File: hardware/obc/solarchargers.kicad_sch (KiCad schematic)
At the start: 35 parts, among them U105 LTC4121, U106 LTC4121

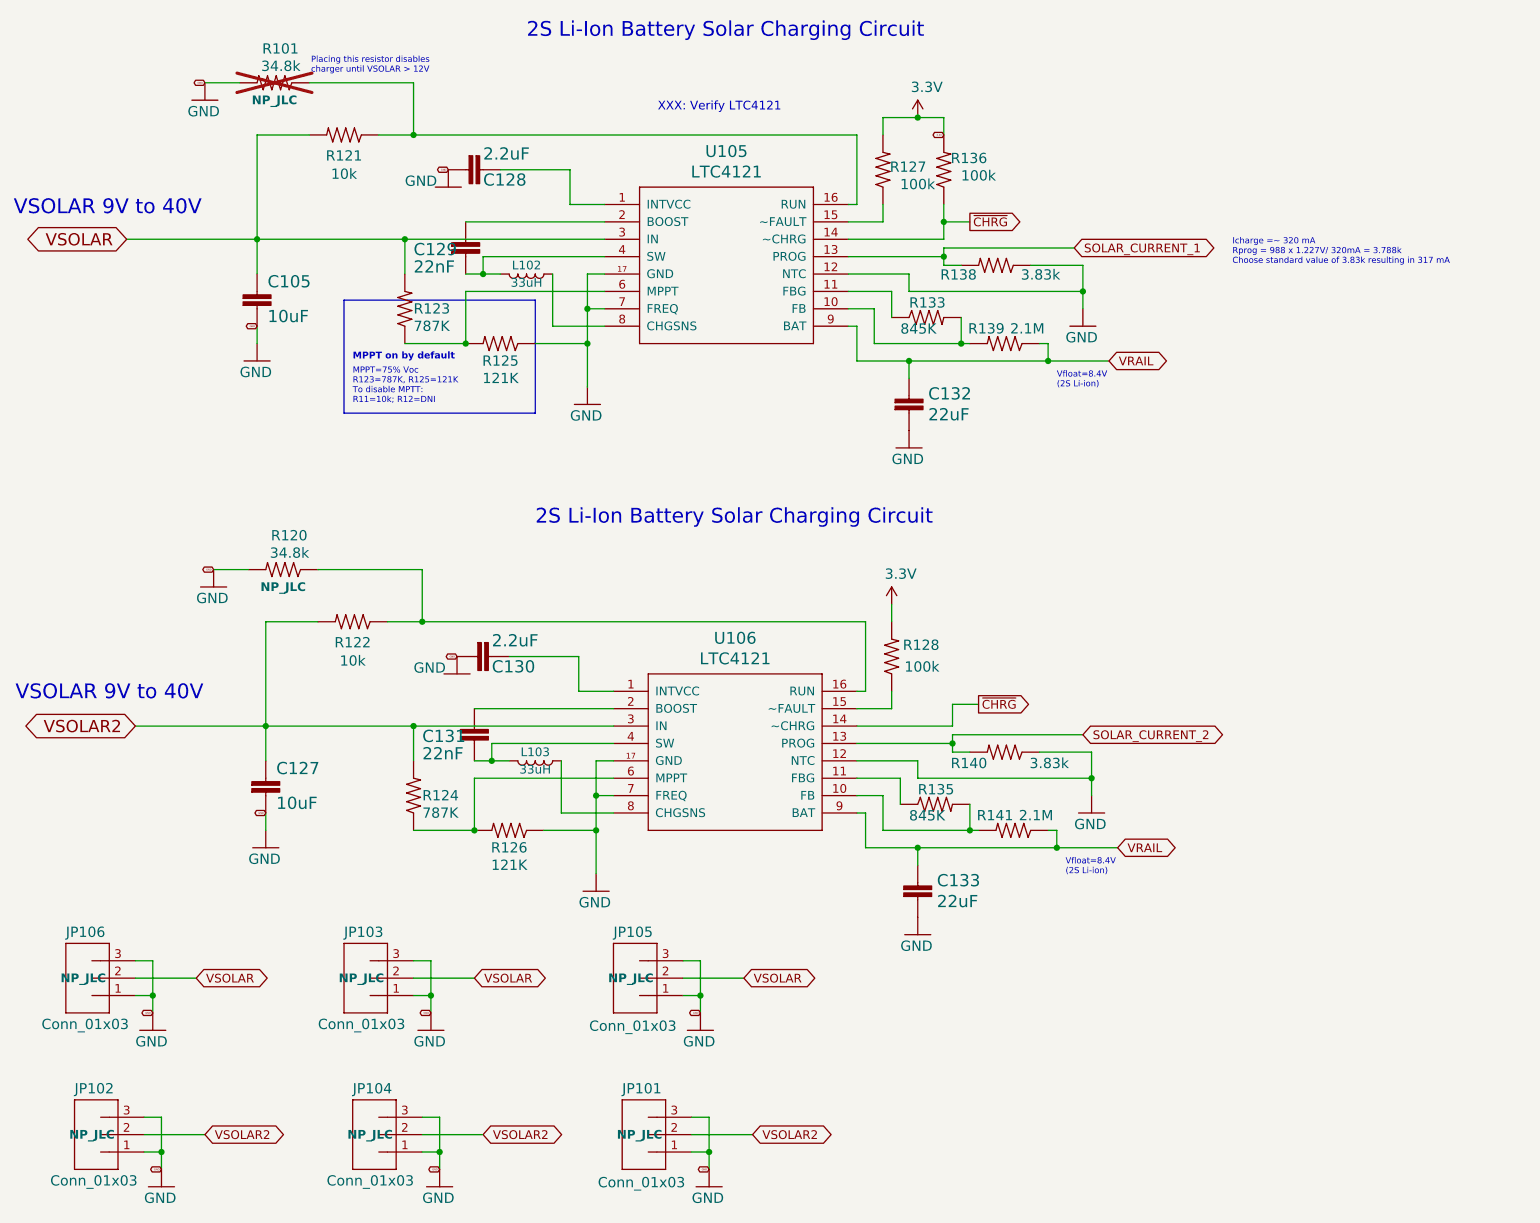
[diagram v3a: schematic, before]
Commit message: obc: design review and corrections
- text cleanup, put components on grid
- Re-route RF power network for radio to get thicker traces and lower
impedance.
- Route RF connections for GPS (controlled impedance)
- Lots of straightening and spreading traces and improving pours
(especially power paths).
- Swap pinning of RBF jumper to reduce the possible downsides of
any shorts or misconnections (don't put pack+ and pack- together on
the connector)
- geographical reannotate
- improve placement of a couple of bypass caps
- Adjust 10uF solar input capacitors to be 35V rated so as to not
limit input voltage.
- fix pinning of RF splitter
- add a couple of STEP models
- obc: add DQ1225 step model
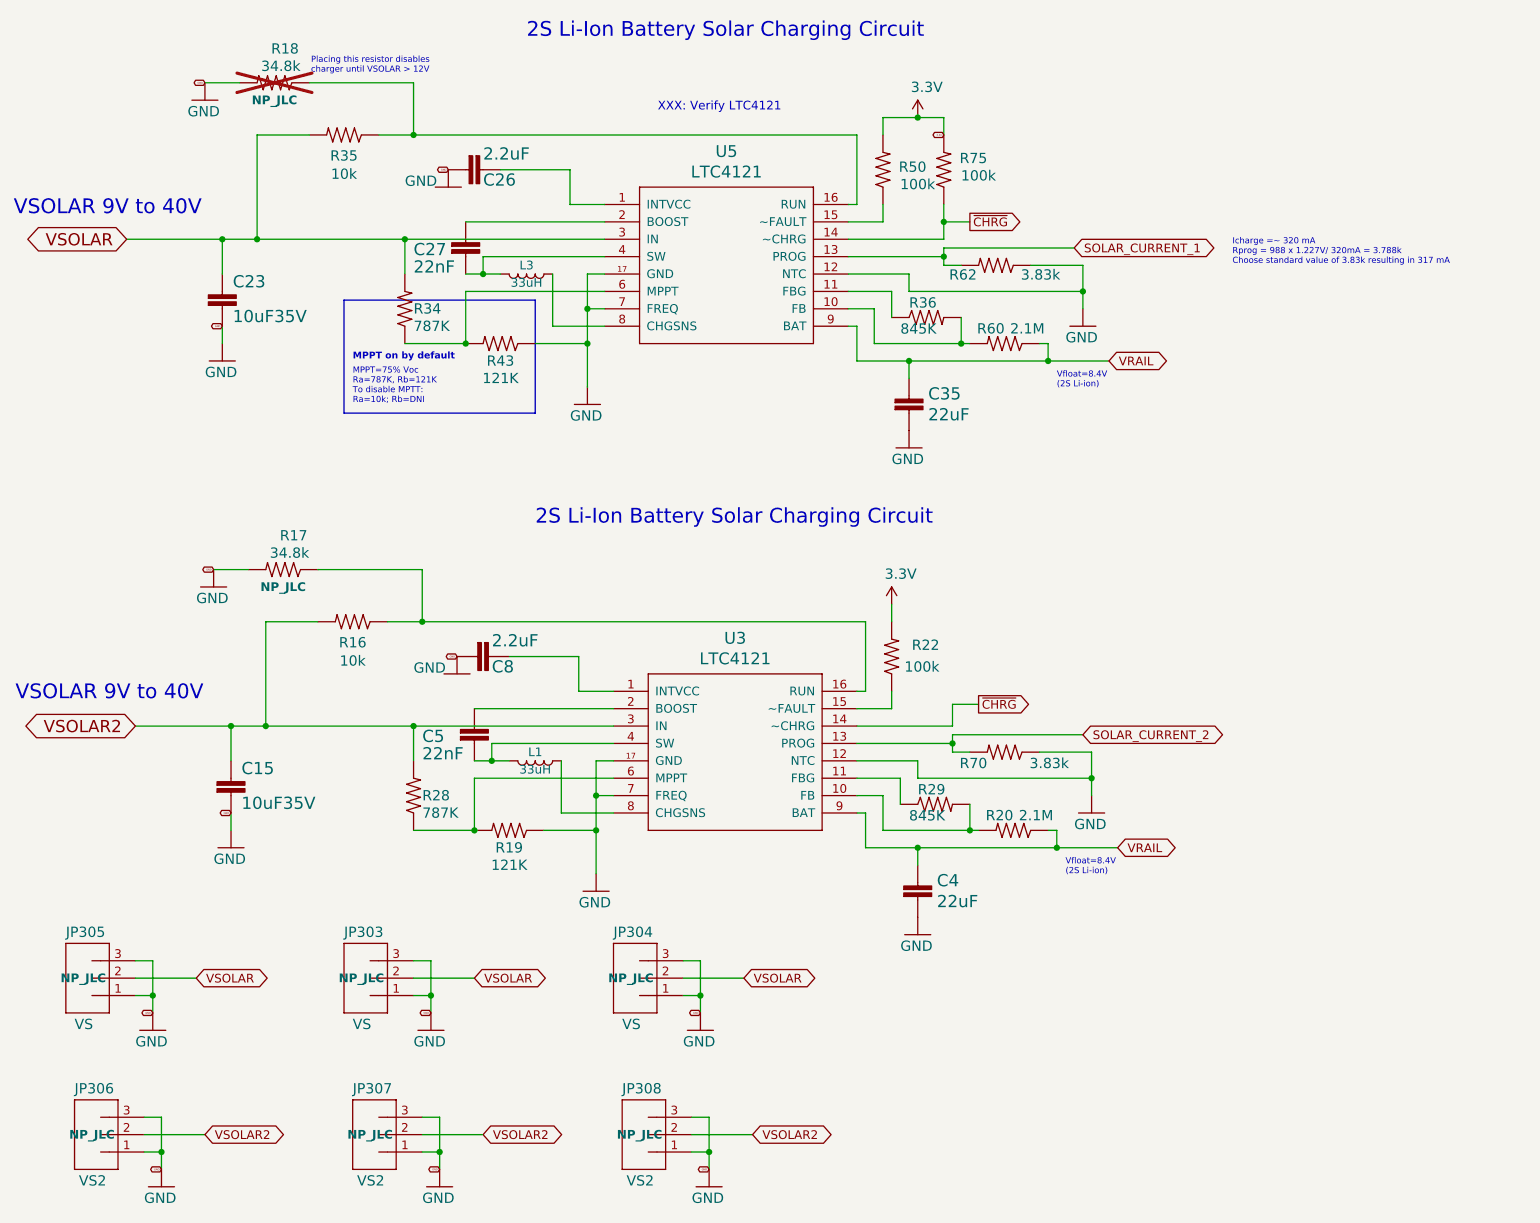
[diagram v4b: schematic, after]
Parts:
- C15: renamed from C127; value 10uF -> 10uF35V; LCSC C344022 -> C194427
- C23: renamed from C105; value 10uF -> 10uF35V; LCSC C344022 -> C194427
- JP303: renamed from JP103; value Conn_01x03 -> VS
- JP304: renamed from JP105; value Conn_01x03 -> VS
- JP305: renamed from JP106; value Conn_01x03 -> VS
- JP306: renamed from JP102; value Conn_01x03 -> VS2
- JP307: renamed from JP104; value Conn_01x03 -> VS2
- JP308: renamed from JP101; value Conn_01x03 -> VS2
- renumbered C128 to C26, C129 to C27, C132 to C35, C133 to C4, C131 to C5, C130 to C8, L103 to L1, L102 to L3, R122 to R16, R120 to R17, R101 to R18, R126 to R19, R141 to R20, R128 to R22, R124 to R28, R135 to R29, R123 to R34, R121 to R35, R133 to R36, R125 to R43, R127 to R50, R139 to R60, R138 to R62, R140 to R70, R136 to R75, U106 to U3, U105 to U5
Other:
- note added: "MPPT=75% Voc Ra=787K, Rb=121K To disable MPTT: Ra=10k; Rb=DNI"
- note removed: "MPPT=75% Voc R123=787K, R125=121K To disable MPTT: R11=10k; R12=DNI"
- moved on the sheet: C15, C23

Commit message: obc: update bom based on availability
IRF7406 -> IRF9393

Change 845k resistor to Panasonic SKU.
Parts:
- R29, R36: LCSC C2091473 -> C416579; Manufacturer_Name (none) -> Panasonic; Manufacturer_Part_Number (none) -> ERJ2RKF8453X
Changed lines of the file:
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@@
 			)
 		)
-		(property "LCSC" "C2091473"
+		(property "LCSC" "C416579"
 			(at 148.59 132.08 0)
 			(effects
@@
 			)
 		)
-		(property "Manufacturer_Name" ""
+		(property "Manufacturer_Name" "Panasonic"
 			(at 148.59 132.08 0)
 			(effects
@@
 			)
 		)
-		(property "Manufacturer_Part_Number" ""
+		(property "Manufacturer_Part_Number" "ERJ2RKF8453X"
 			(at 148.59 132.08 0)
 			(effects
@@
 			)
 		)
-		(property "LCSC" "C2091473"
+		(property "LCSC" "C416579"
 			(at 147.32 60.96 0)
 			(effects
@@
 			)
 		)
-		(property "Manufacturer_Name" ""
+		(property "Manufacturer_Name" "Panasonic"
 			(at 147.32 60.96 0)
 			(effects
@@
 			)
 		)
-		(property "Manufacturer_Part_Number" ""
+		(property "Manufacturer_Part_Number" "ERJ2RKF8453X"
 			(at 147.32 60.96 0)
 			(effects
